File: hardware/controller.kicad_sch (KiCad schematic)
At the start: 43 parts, among them J1 Connector, USB-TYPE-C-16P, U1 ESP32-C6-WROOM-1, U2 MCP73871-1AA, U3 TPS62840YBGR

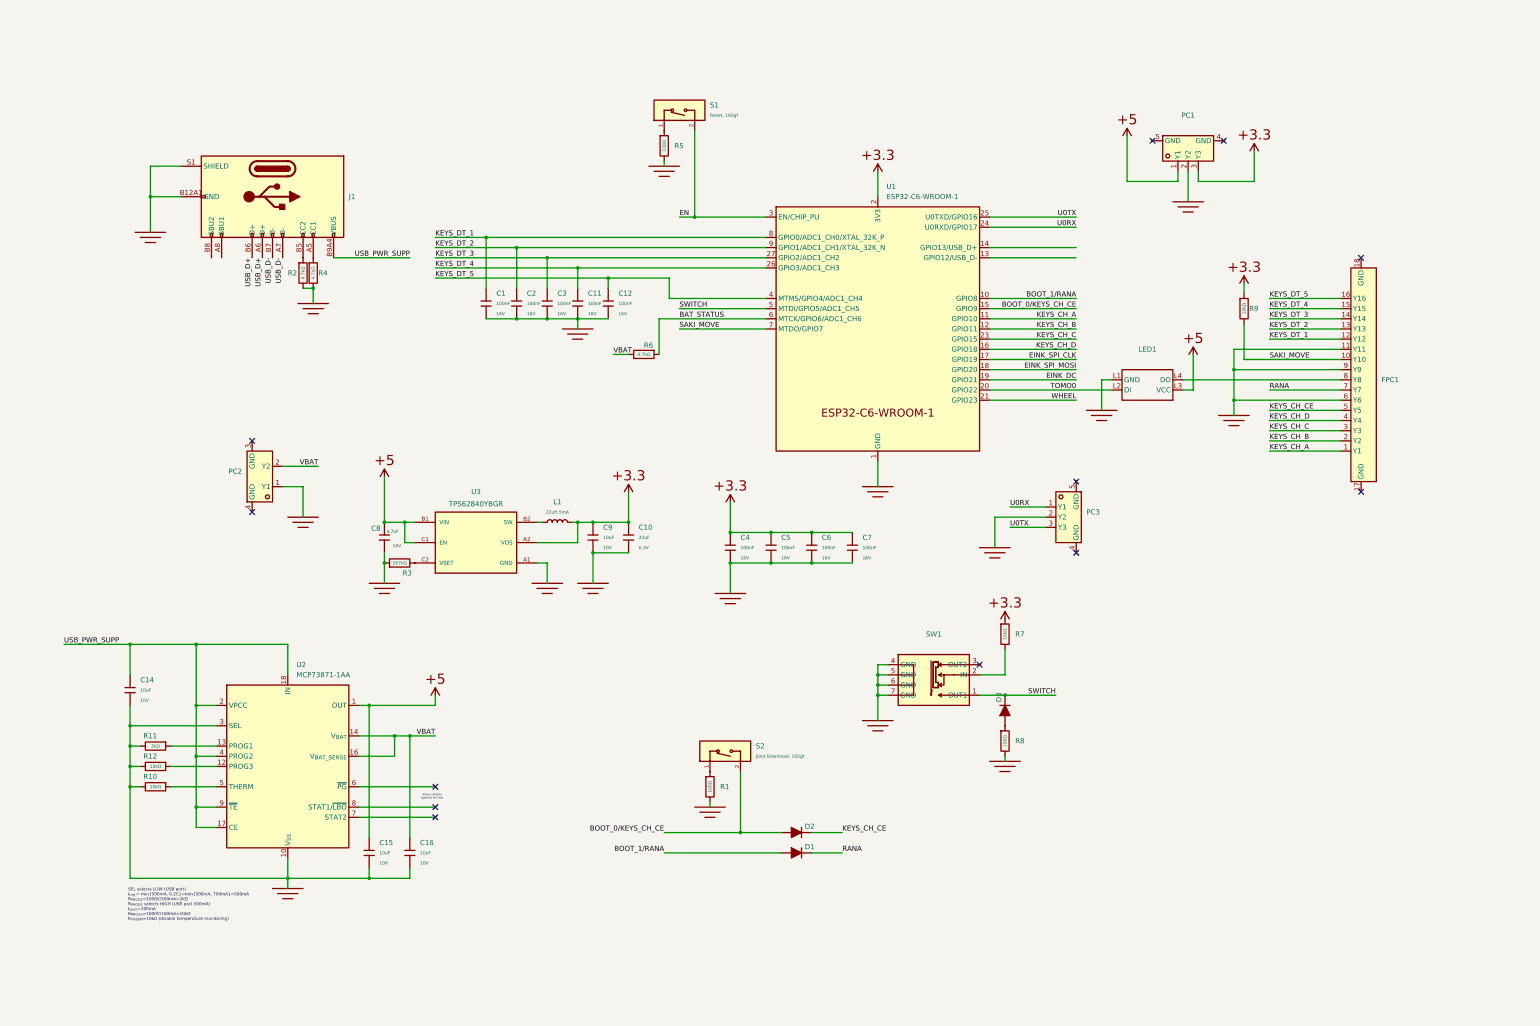
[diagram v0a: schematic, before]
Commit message: :sparkles: USB hub & USB2UART
Signed-off-by: symlpigeon <symlpigeon@foxmail.com>
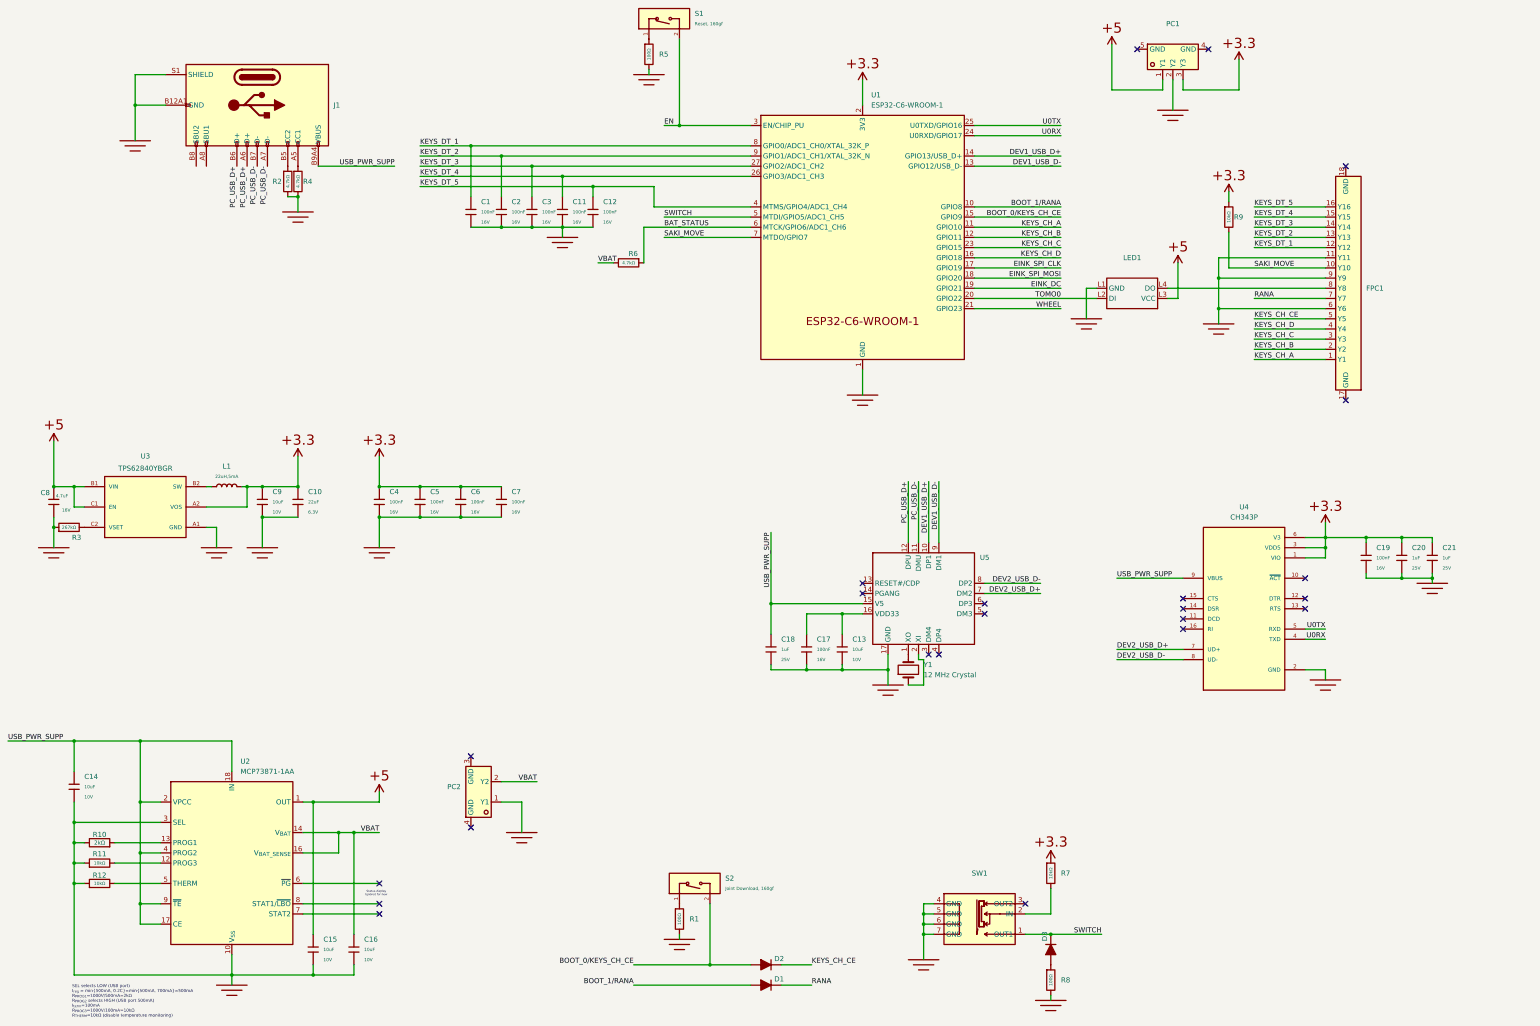
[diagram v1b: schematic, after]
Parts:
- removed PC3: ~, KeysDock:ZX-ZH1.5-3PWT, symbol components:ZX-ZH1.5-3PWT
- removed R10, R12: 10kΩ, KeysDock:R_0402, symbol components:0402,267kΩ
- removed R11: 2kΩ, KeysDock:R_0402, symbol components:0402,267kΩ
- added C13: 10uF, KeysDock:C_0603, symbol components:0603,10uF
- added C17, C19: 100nF, KeysDock:C_0402, symbol components:0402,100nF
- added C18, C20, C21: 1uF, KeysDock:C_0402, symbol components:0402,1uF
- added R10: 2kΩ, symbol Device:R
- added R11, R12: 10kΩ, KeysDock:R_0402, symbol components:0402,10kΩ
- added U4: CH343P, KeysDock:QFN50P300X300X80-17N, symbol components:CH343P
- added U5: ~, KeysDock:QFN50P300X300X80-17N, symbol components:CH334P
- added Y1: 12 MHz Crystal, symbol Device:Crystal
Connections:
- net P,+3.3: now also C19.2, C20.1, C21.1, U4.1 (VIO), U4.3 (VDD5), U4.6 (V3)
- net P,E: now also C13.2, C17.2, C18.2, C19.1, C20.2, C21.2, R10.1, R11.1, R12.1, U4.2 (GND), U5.17 (GND)
- net U0RX: now also U4.4 (TXD)
- net U0TX: now also U4.5 (RXD)
- net USB_PWR_SUPP: now also C18.1, U4.9 (VBUS), U5.15 (V5)
- net at U2.12 (PROG3): now also R11.2
- net at U2.13 (PROG1): now also R10.2
- net at U2.5 (THERM): now also R12.2
- net DEV1_USB_D-: now reaches U1.13 (GPIO12/USB_D-)
- net DEV1_USB_D-: now also U5.9 (DM1)
- net DEV1_USB_D+: now reaches U1.14 (GPIO13/USB_D+)
- net DEV1_USB_D+: now also U5.10 (DP1)
- net USB_D+ renamed PC_USB_D+
- net PC_USB_D+: now also U5.12 (DPU)
- net USB_D- renamed PC_USB_D-
- net PC_USB_D-: now also U5.11 (DMU)
- new net: C13.1, C17.1, U5.16 (VDD33)
- new net: U5.1 (XO), Y1.2
- new net: U5.2 (XI), Y1.1
- new net DEV2_USB_D+: U4.7 (UD+), U5.7 (DM2)
- new net DEV2_USB_D-: U4.8 (UD-), U5.8 (DP2)
- new net GND: U4.17 (GND)
- no-connect marks 12 -> 23
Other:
- moved on the sheet: C1, C10, C11, C12, C14, C15, C16, C2, C3, C4, C5, C6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

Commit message: :construction: change power ic & switch
Signed-off-by: symlpigeon <symlpigeon@foxmail.com>
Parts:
- removed U2: MCP73871-1AA, Package_DFN_QFN:QFN-20-1EP_4x4mm_P0.5mm_EP2.5x2.5mm, symbol Battery_Management:MCP73871-1AA
- added D4: SM4007PL, KeysDock:D_SOD-123FL, symbol components:SM4007PL
- added SW2: ~, KeysDock:SW-SMD_SSSS811101, symbol components:SSSS811101
- added U6: MCP73871-2CC, Package_DFN_QFN:QFN-20-1EP_4x4mm_P0.5mm_EP2.5x2.5mm, symbol Battery_Management:MCP73871-2CC
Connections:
- net P,+5: now also U6.1 (OUT), U6.20 (OUT)
- net P,E: now also SW2.4 (GND), SW2.5 (GND), SW2.6 (GND), SW2.7 (GND), U6.10 (V_{SS}), U6.11 (V_{SS}), U6.21 (V_{SS}), U6.3 (SEL)
- net USB_PWR_SUPP: now also U6.17 (CE), U6.18 (IN), U6.19 (IN), U6.2 (VPCC), U6.4 (PROG2), U6.9 (~{TE})
- net VBAT: now also SW2.2 (IN), U6.16 (V_{BAT_SENSE}); no longer C16.1
- net at R11.2: now also U6.12 (PROG3)
- net at R10.2: now also U6.13 (PROG1)
- net at R12.2: now also U6.5 (THERM)
- new net: C16.1, D4.2 (A), SW2.3 (OUT2), U6.14 (V_{BAT}), U6.15 (V_{BAT})
- new net: D4.1 (K), SW2.1 (OUT1)
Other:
- moved on the sheet: PC2

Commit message: :construction: try construct power supply & charging
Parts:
- removed C1, C11, C12, C2, C3: 100nF, KeysDock:C_0402, symbol components:0402,100nF
- removed C14, C15, C16, C9: 10uF, KeysDock:C_0603, symbol components:0603,10uF
- removed C8: 4.7uF, KeysDock:C_0603, symbol components:0603,4.7uF
- removed D2, D3, D4: SM4007PL, KeysDock:D_SOD-123FL, symbol components:SM4007PL
- removed R1, R8: 100Ω, KeysDock:R_0402, symbol components:0402,100Ω
- removed R10: 2kΩ, symbol Device:R
- removed R11, R12, R7: 10kΩ, KeysDock:R_0402, symbol components:0402,10kΩ
- removed R3: 267kΩ, KeysDock:R_0402, symbol components:0402,267kΩ
- removed R6: 4.7kΩ, KeysDock:R_0402, symbol components:0402,4.7kΩ
- removed S2: Joint Download, 160gf, KeysDock:SW_TS-1088-AR02016, symbol components:Tactile Button, 160gf, 12V, 50mA, 4.0mm
- removed SW2: ~, KeysDock:SW-SMD_SSSS811101, symbol components:SSSS811101
- removed U3: TPS62840YBGR, KeysDock:BGA6N40P3X2_146X96X50N, symbol components:TPS62840YBGR
- removed U6: MCP73871-2CC, Package_DFN_QFN:QFN-20-1EP_4x4mm_P0.5mm_EP2.5x2.5mm, symbol Battery_Management:MCP73871-2CC
- added C1, C14: 4.7uF, KeysDock:C_0402, symbol components:0402,4.7uF
- added C11, C15, C2, C3: 1uF, KeysDock:C_0402, symbol components:0402,1uF
- added C8: 10uF, KeysDock:C_0402, symbol components:0402,10uF
- added C9: 3.3nF, KeysDock:C_0402, symbol components:0402,3.3nF
- added R10: 0Ω, KeysDock:R_0402, symbol components:0402,0Ω
- added R3: 100kΩ, KeysDock:R_0402, symbol components:0402,100kΩ
- added R6: 100Ω, KeysDock:R_0402, symbol components:0402,100Ω
- added S3: Joint Download, 160gf, KeysDock:SW_TS-1088-AR02016, symbol components:Tactile Button, 160gf, 12V, 50mA, 4.0mm
- added U2: BQ24074RGTR, KeysDock:QFN50P300X300X80-17N, symbol components:BQ24074RGTR
- added U3: TLA2518IRTER, KeysDock:QFN50P300X300X80-17N, symbol components:TLA2518IRTER
- added U6: TPS62142RGTR, KeysDock:QFN50P300X300X80-17N, symbol components:TPS62142RGTR
- L1: value 22uH,5mA -> 2.2uH,5mA
- U1: 技术规格 (none) -> ${KIPRJMOD}/docs/esp32-c6-technical-reference-manual-cn.pdf
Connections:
- net EINK_DC is gone; now on net RANA: U1.19 (GPIO21)
- net KEYS_CH_CE: now also U1.21 (GPIO23)
- net KEYS_DT_1: now also U3.1 (AIN2/GPIO2); no longer U1.8 (GPIO0/ADC1_CH0/XTAL_32K_P)
- net KEYS_DT_2: now also U3.2 (AIN3/GPIO3); no longer U1.9 (GPIO1/ADC1_CH1/XTAL_32K_N)
- net KEYS_DT_3: now also U3.3 (AIN4/GPIO4); no longer U1.27 (GPIO2/ADC1_CH2)
- net KEYS_DT_4: now also U3.4 (AIN5/GPIO5); no longer U1.26 (GPIO3/ADC1_CH3)
- net KEYS_DT_5: now also U3.5 (AIN6/GPIO6); no longer U1.4 (MTMS/GPIO4/ADC1_CH4)
- net P,+3.3: now also C11.2, C2.1, R3.1, U3.10 (DVDD), U3.7 (AVDD), U6.14 (VOS)
- net P,+5: now also C14.2, C8.1, U2.10 (OUT_10), U2.11 (OUT_11), U2.5 (EN2), U6.10 (AVIN), U6.11 (PVIN_11), U6.12 (PVIN_12), U6.13 (EN)
- net P,E: now also C1.1, C14.1, C15.2, C8.2, C9.2, R10.2, R6.2, U2.14 (TMR), U2.17 (EXP), U2.4 (~{CE}), U2.6 (EN1), U2.8 (VSS), U6.15 (PGND_15), U6.16 (PGND_16), U6.17 (EXP), U6.5 (FB), U6.7 (FSW), U6.8 (DEF)
- net RANA: no longer D1.1 (K)
- net SAKI_MOVE: now also U1.26 (GPIO3/ADC1_CH3); no longer U1.7 (MTDO/GPIO7)
- net USB_PWR_SUPP: now also C15.1, U2.13 (IN)
- net VBAT: now also SW1.2 (IN), C1.2, U2.2 (BAT_2), U2.3 (BAT_3), U3.6 (AIN7/GPIO7); no longer PC2.2 (Y2)
- net WHEEL: now also U1.4 (MTMS/GPIO4/ADC1_CH4); no longer U1.21 (GPIO23)
- net at SW1.3 (OUT2): now also D1.2 (A)
- net at L1.1: now also U6.1 (SW_1), U6.2 (SW_2), U6.3 (SW_3)
- net HID_USB_D-: now reaches U5.3 (DM4)
- net HID_USB_D-: now also U1.13 (GPIO12/USB_D-)
- net HID_USB_D+: now reaches U5.4 (DP4)
- net HID_USB_D+: now also U1.14 (GPIO13/USB_D+)
- net BAT_STATUS renamed SPI_CLK
- net SPI_CLK: now also U3.13 (SCLK)
- net BOOT_0/KEYS_CH_CE renamed BOOT_0
- net BOOT_0: now also S3.2 (B)
- net BOOT_1/RANA renamed BOOT_1
- net BOOT_1: no longer D1.2 (A)
- net DEV1_USB_D+: no longer names the net of U5.10 (DP1)
- net DEV1_USB_D+: no longer U1.14 (GPIO13/USB_D+)
- net DEV1_USB_D-: no longer names the net of U5.9 (DM1)
- net DEV1_USB_D-: no longer U1.13 (GPIO12/USB_D-)
- net DEV2_USB_D+ renamed U0_USB_D+
- net U0_USB_D+: now also U5.8 (DP2); no longer U5.7 (DM2)
- net DEV2_USB_D- renamed U0_USB_D-
- net U0_USB_D-: now also U5.7 (DM2); no longer U5.8 (DP2)
- net EINK_SPI_CLK renamed SPI_CS3_ADC
- net SPI_CS3_ADC: now also U3.11 (*CS)
- net EINK_SPI_MOSI renamed SPI_CS4_EINK
- net SWITCH: no longer names the net of SW1.1 (OUT1)
- net SWITCH: now also D1.1 (K), PC2.2 (Y2); no longer U1.5 (MTDI/GPIO5/ADC1_CH5)
- new net: R6.1, S3.1 (A)
- new net: C3.1, U3.8 (DECAP)
- new net: C9.1, U6.9 (SS/TR)
- new net: R3.2, U6.4 (PG)
- new net BAT_CHG: U1.5 (MTDI/GPIO5/ADC1_CH5), U2.9 (~{CHG})
- new net P,GND: C11.1, C2.2, C3.2, R10.1, U3.15 (AIN0/GPIO0), U3.16 (AIN1/GPIO1), U3.17 (GND), U3.9 (GND), U6.6 (AGND)
- new net SPI_MISO: U1.27 (GPIO2/ADC1_CH2), U3.12 (SDO)
- new net SPI_MOSI: U1.7 (MTDO/GPIO7), U3.14 (SDI)
- no-connect marks 23 -> 20
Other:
- note added: "GNDA"
- note added: "GNDD"
- note added: "GND_BAT"
- note removed: "SEL selects LOW (USB port) I_{reg} = min{500mA, 0.2C}=min{500mA, 700mA}=500mA R_{PROG1}=1000V/500mA=2kΩ R_{PROG2} selects HIGH (USB port 500mA) I_{term}=100mA R_{PROG3}=1000V/100mA=10kΩ R_{THERM}=10kΩ (disable temperature monitoring)"
- note removed: "Status display Ignored for now"
- moved on the sheet: C13, C17, C18, C19, C20, C21, C4, C5, C6, C7, FPC1, J1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

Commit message: :sparkles: refine capacitors and crystals, finish charge chip
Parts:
- removed Y1: 12 MHz Crystal, symbol Device:Crystal
- added R1: 10kΩ, KeysDock:R_0402, symbol components:0402,10kΩ
- added R11: 3kΩ, KeysDock:R_0402, symbol components:0402,3kΩ
- added R7: 1.78kΩ, KeysDock:R_0402, symbol components:0402,1.78kΩ
- added R8: 1.54kΩ, KeysDock:R_0402, symbol components:0402,1.54kΩ
- added X1: 12MHz, PCM_Crystal_AKL:Crystal_SMD_3225-4Pin_3.2x2.5mm, symbol components:YXC-YSO110TR
- C10: footprint KeysDock:C_0603 -> KeysDock:C_0402; symbol components:0603,22uF -> components:0402,22uF; LCSC C59461 -> C105226; Part CL10A226MQ8NRNC -> CL05A226MQ5QUNC; Price 0.012USD -> 0.009USD; Stock 5081183 -> 3940889
- C13: footprint KeysDock:C_0603 -> KeysDock:C_0402; symbol components:0603,10uF -> components:0402,10uF; LCSC C19702 -> C15525; Part CL10A106KP8NNNC -> CL05A106MQ5NUNC; Stock 9881407 -> 3940889; Tolerance ±10% -> ±20%; Voltage Rated 10V -> 6.3V
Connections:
- net P,E: now also R1.1, R11.2, R7.1, R8.1
- net at U2.1 (TS): now also R1.2
- net at U2.12 (ILIM): now also R8.2
- net at U2.15 (ITERM): now also R11.1
- net at U2.16 (ISET): now also R7.2
- net at U5.1 (XO): now also X1.3
- net at U5.2 (XI): now also X1.1
- new net P,0: X1.2, X1.4
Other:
- moved on the sheet: C15
